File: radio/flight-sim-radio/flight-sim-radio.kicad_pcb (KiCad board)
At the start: 2 copper layers, 170 x 45 mm, 30 parts, among them J1 Conn_01x03, J2 Conn_01x09, J3 Conn_01x04, SW1 RS-08 300±150GF, SW2 RotaryEncoder_Switch, SW3 RotaryEncoder_Switch, U1 74LS148, U2 TM1637, U3 TM1637

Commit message: First driver layed out
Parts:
- removed U2: TM1637, Package_DIP:DIP-20_W7.62mm
- added U4: TM1638, radio_footprints:TM1638, F.Cu at (107.0, 120.0)
- U3: value TM1637 -> TM1638; footprint Package_DIP:DIP-20_W7.62mm -> radio_footprints:TM1638
- moved C5 101.7 mm to (120.7, 34.6), turned to 0 degrees
- moved C3 90.2 mm to (120.9, 45.0), turned to 0 degrees
- moved U3 84.9 mm to (109.2, 38.8), turned to 0 degrees
- moved C6 9.95 mm to (123.0, 115.5)
- moved C4 9.47 mm to (118.5, 115.2)
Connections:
- U3 pad 1: GND -> unconnected-(U3-K1-Pad1)
- U3 pad 10: /D2_GRID6 -> /D1_SEG6
- U3 pad 11: /D2_GRID5 -> /D1_SEG7
- U3 pad 12: /D2_GRID4 -> /D1_SEG8
- U3 pad 13: /D2_GRID3 -> unconnected-(U3-SEG9-Pad13)
- U3 pad 14: /D2_GRID2 -> unconnected-(U3-SEG10-Pad14)
- U3 pad 15: /D2_GRID1 -> VDD
- U3 pad 16: VDD -> unconnected-(U3-GRID8-Pad16)
- U3 pad 17: /D2_DIO -> unconnected-(U3-GRID7-Pad17)
- U3 pad 18: /D2_CLK -> GND
- U3 pad 19: unconnected-(U3-K1-Pad19) -> /D1_GRID6
- U3 pad 2: /D2_SEG1 -> unconnected-(U3-K2-Pad2)
- U3 pad 20: unconnected-(U3-K2-Pad20) -> /D1_GRID5
- U3 pad 3: /D2_SEG2 -> unconnected-(U3-K3-Pad3)
- U3 pad 4: /D2_SEG3 -> VDD
- U3 pad 5: /D2_SEG4 -> /D1_SEG1
- U3 pad 6: /D2_SEG5 -> /D1_SEG2
- U3 pad 7: /D2_SEG6 -> /D1_SEG3
- U3 pad 8: /D2_SEG7 -> /D1_SEG4
- U3 pad 9: /D2_SEG8 -> /D1_SEG5
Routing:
- net GND: track 306.7 -> 179.9 mm
- net VDD: track 246.8 -> 163.7 mm
- net /D1_SEG7: track 53.2 -> 0.00 mm
- net /D1_SEG1: track 38.1 -> 0.00 mm
- net /D1_SEG6: track 34.4 -> 0.00 mm
- net /D1_GRID4: track 31.2 -> 0.00 mm
- net /D1_SEG5: track 30.2 -> 0.00 mm
- net /D1_GRID6: track 27.3 -> 0.00 mm
- net /D2_SEG7: track 52.9 -> 25.8 mm, vias 0 -> 2
- net /D1_GRID1: track 26.5 -> 0.00 mm, vias 1 -> 0
- net /D1_SEG3: track 24.4 -> 0.00 mm
- net /D1_SEG2: track 24.4 -> 0.00 mm, vias 1 -> 0
- net /D1_GRID5: track 23.5 -> 0.00 mm
- net /D1_DIO: track 27.9 -> 5.61 mm
- net /D1_CLK: track 32.8 -> 10.7 mm
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
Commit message: PCB complete
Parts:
- removed R8, R9: 10k, Resistor_THT:R_Axial_DIN0207_L6.3mm_D2.5mm_P10.16mm_Horizontal
- moved C5 95.4 mm to (172.0, 115.0), turned to -90 degrees
- moved U3 91.9 mm to (152.2, 120.0)
- moved C3 84.0 mm to (167.7, 114.8), turned to -90 degrees
- moved R6 9.09 mm to (133.5, 124.1), turned to 90 degrees
- moved R7 8.40 mm to (130.5, 124.1), turned to 90 degrees
- moved J3 3.05 mm to (136.3, 127.1)
- moved D1 0.14 mm to (154.5, 105.3)
- moved D2 0.12 mm to (109.3, 105.4)
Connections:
- J3 pad 1: /D1_DIO -> /D_DIO
- J3 pad 2: /D1_CLK -> /D_CLK
- J3 pad 3: /D2_DIO -> /D1_STB
- J3 pad 4: /D2_CLK -> /D2_STB
- R6 pad 1: /D1_CLK -> /D_DIO
- R7 pad 1: /D1_DIO -> /D_CLK
- U3 pad 26: /D1_DIO -> /D_DIO
- U3 pad 27: /D1_CLK -> /D_CLK
- U3 pad 28: unconnected-(U3-STB-Pad28) -> /D1_STB
- U4 pad 26: /D2_DIO -> /D_DIO
- U4 pad 27: /D2_CLK -> /D_CLK
- U4 pad 28: unconnected-(U4-STB-Pad28) -> /D2_STB
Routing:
- net /D_DIO: track 0.00 -> 66.6 mm, vias 0 -> 1
- net /D_CLK: track 0.00 -> 61.4 mm
- net GND: track 179.9 -> 237.0 mm
- net VDD: track 163.7 -> 218.4 mm, vias 0 -> 2
- net /D2_DIO: track 42.6 -> 0.00 mm
- net /D2_STB: track 0.00 -> 36.9 mm
- net /D2_CLK: track 36.4 -> 0.00 mm
- net /D1_SEG1: track 0.00 -> 34.5 mm, vias 0 -> 1
- net /D1_SEG6: track 0.00 -> 32.8 mm, vias 0 -> 1
- net /D1_SEG2: track 0.00 -> 28.1 mm, vias 0 -> 1
- net /D1_STB: track 0.00 -> 27.5 mm, vias 0 -> 1
- net /D1_SEG3: track 0.00 -> 27.0 mm, vias 0 -> 1
- net /D1_SEG7: track 0.00 -> 25.8 mm, vias 0 -> 2
- net /D1_SEG5: track 0.00 -> 24.2 mm, vias 0 -> 2
- net /D1_GRID6: track 0.00 -> 23.7 mm
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
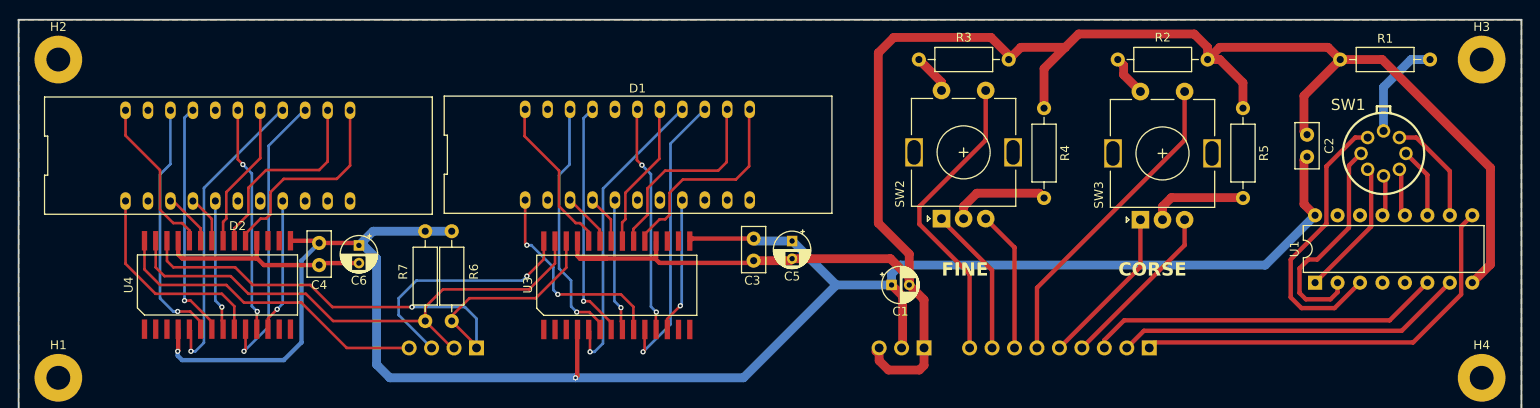
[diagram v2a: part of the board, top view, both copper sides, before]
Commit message: Update silk screen
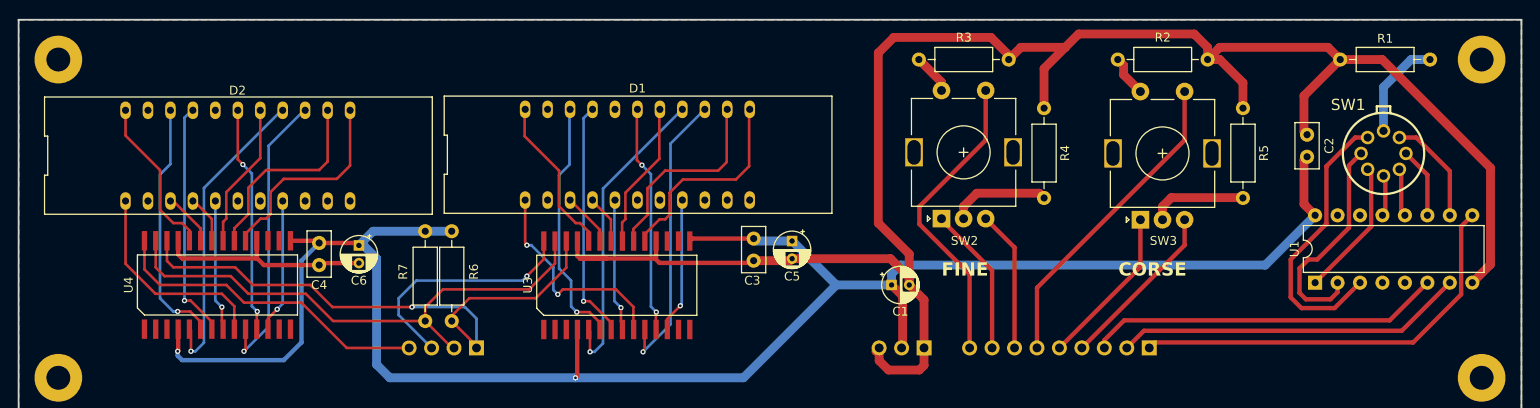
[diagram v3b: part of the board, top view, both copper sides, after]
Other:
- board text added: "CLK"
- board text added: "D1"
- board text added: "D2"
- board text added: "DIO"
- board text removed: "D1C"
- board text removed: "D1D"
- board text removed: "D2C"
- board text removed: "D2D"
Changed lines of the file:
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@@
 			(at 0 -3.7 0)
 			(layer "F.SilkS")
+			(hide yes)
 			(effects
 				(font
@@
 		(tags "rotary encoder")
 		(property "Reference" "SW2"
-			(at 2.8 -4.7 90)
+			(at -2.5 2.6 180)
 			(layer "F.SilkS")
 			(effects
@@
 		(tags "mounting hole 2.7mm m2.5")
 		(property "Reference" "H3"
-			(at 0 -3.7 0)
+			(at 0 4 0)
 			(layer "F.SilkS")
+			(hide yes)
 			(effects
 				(font
@@
 		(tags "6 Digit 7 Segment Display")
 		(property "Reference" "D2"
-			(at -0.035 7.95 0)
+			(at -0.035 -7.37 0)
 			(layer "F.SilkS")
 			(effects
@@
 		(tags "rotary encoder")
 		(property "Reference" "SW3"
-			(at 2.8 -4.7 90)
+			(at -2.38 2.6 180)
 			(layer "F.SilkS")
 			(effects
@@
 		(tags "mounting hole 2.7mm m2.5")
 		(property "Reference" "H2"
-			(at 0 -3.7 0)
+			(at 4.5 0 0)
 			(layer "F.SilkS")
+			(hide yes)
 			(effects
 				(font
@@
 			(at 0 -3.7 0)
 			(layer "F.SilkS")
+			(hide yes)
 			(effects
 				(font
@@
 		(tags "Through hole pin header THT 1x03 2.54mm single row")
 		(property "Reference" "J1"
-			(at 0 2.33 90)
+			(at 0.12 2.575 90)
 			(layer "B.SilkS")
 			(effects
@@
 		)
 	)
-	(gr_text "D1D"
+	(gr_text "DIO"
 		(at 135.55 133.5 270)
 		(layer "B.SilkS")
@@
 		)
 	)
-	(gr_text "D1C"
+	(gr_text "CLK"
 		(at 132.8 133.5 270)
 		(layer "B.SilkS")
@@
 		)
 	)
-	(gr_text "D2D"
+	(gr_text "D1"
 		(at 130.3 133.5 270)
 		(layer "B.SilkS")
@@
 		)
 	)
-	(gr_text "D2C"
+	(gr_text "D2"
 		(at 127.55 133.5 270)
 		(layer "B.SilkS")
@@
 	)
 	(segment
-		(start 145.5 121.067724)
-		(end 152.640908 121.067724)
+		(start 146.067724 120.5)
+		(end 152.073184 120.5)
 		(width 0.3)
 		(layer "F.Cu")
@@
 	)
 	(segment
-		(start 154.045908 122.472724)
-		(end 154.045908 125.067724)
+		(start 141.805688 110.39435)
+		(end 141.805688 115.305688)
 		(width 0.3)
 		(layer "F.Cu")
@@
 	)
 	(segment
-		(start 141.805688 110.39435)
-		(end 141.805688 115.305688)
+		(start 145.5 121.067724)
+		(end 146.067724 120.5)
 		(width 0.3)
 		(layer "F.Cu")
@@
 	)
 	(segment
-		(start 141.805688 115.305688)
-		(end 142 115.5)
+		(start 152.073184 120.5)
+		(end 154.045908 122.472724)
 		(width 0.3)
 		(layer "F.Cu")
@@
 	)
 	(segment
-		(start 152.640908 121.067724)
-		(end 154.045908 122.472724)
+		(start 154.045908 122.472724)
+		(end 154.045908 125.067724)
+		(width 0.3)
+		(layer "F.Cu")
+		(net 4)
+	)
+	(segment
+		(start 141.805688 115.305688)
+		(end 142 115.5)
 		(width 0.3)
 		(layer "F.Cu")
